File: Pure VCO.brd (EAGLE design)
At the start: 68.8 x 100 mm, 118 parts, among them IC1 TL072, IC2 TL072, IC3 TL072, IC4 TL072, IC5 TL072, IC6 TL072, IC7 TL072, IC8 LM4040A50IDBZT, T1 MMBFJ309

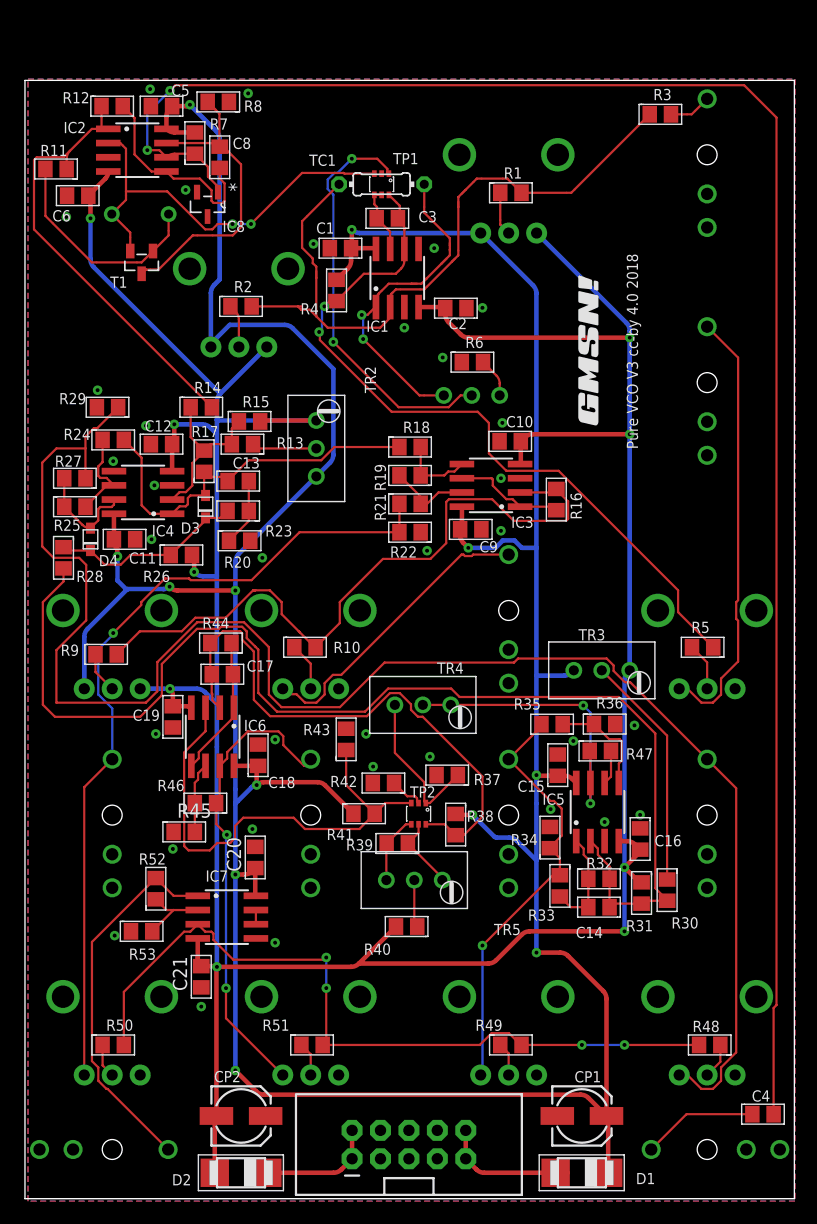
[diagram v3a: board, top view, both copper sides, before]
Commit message: VCO 3.1
VCO Updated to V3.1 14/04/21.

Mixer section changed from Average to Sum. Mix Out is now inversion of individual outs. Might be useful?
Resistor values around mixer section reduced to 10k, inline with low noise techniques.
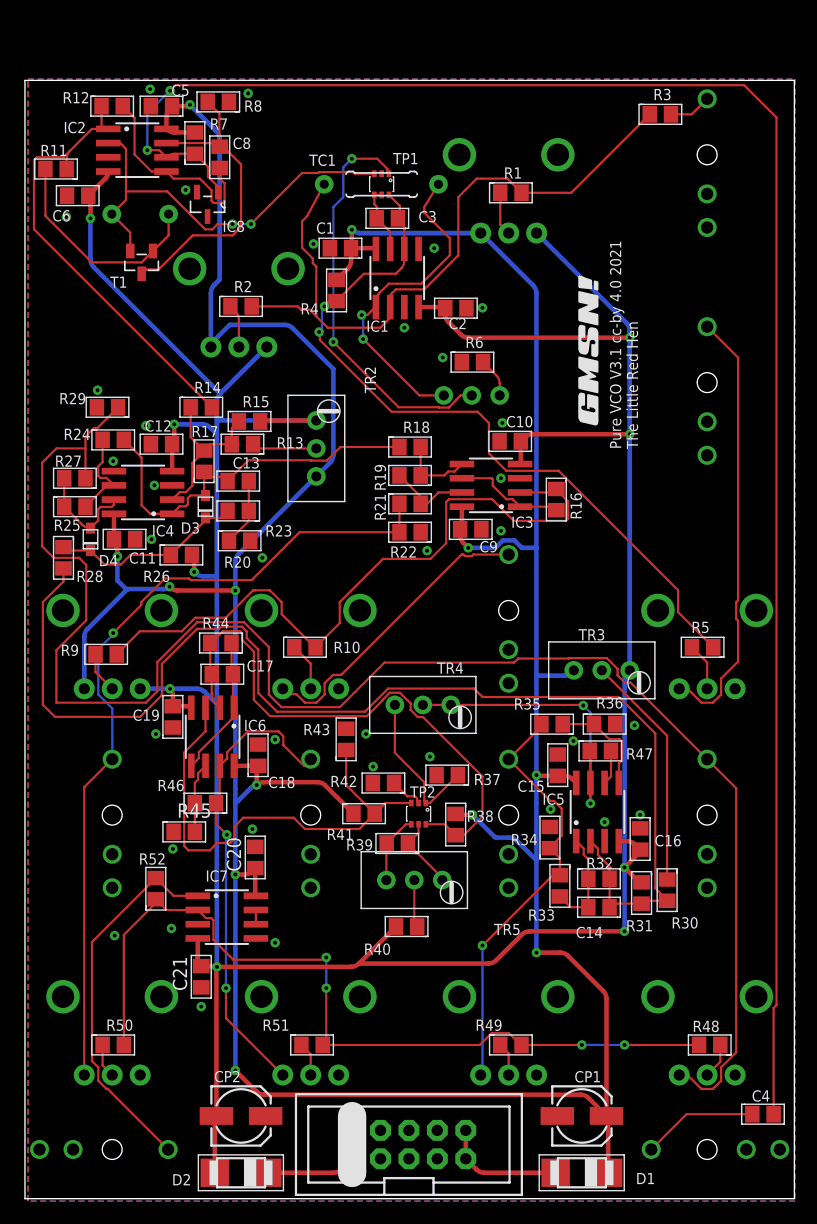
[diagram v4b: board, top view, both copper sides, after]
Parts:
- removed R53: 100k, GMSN:R0805
- COARSE: device GMSN:POTENTIOMETER_9MM -> GMSN:POT_9MM_RED_KNOB
- FINE: device GMSN:POTENTIOMETER_9MM -> GMSN:POT_9MM_RED_MXR_KNOB
- FM_LEVEL, PWM_LEVEL: device GMSN:POTENTIOMETER_9MM -> GMSN:POT_9MM_GREEN_KNOB
- PULSE_MIX, SAW_MIX, SINE_MIX, TRI_MIX: device GMSN:POTENTIOMETER_9MM -> GMSN:POT_9MM_BLUE_KNOB
- PULSE_WIDTH: device GMSN:POTENTIOMETER_9MM -> GMSN:POT_9MM_YELLOW_KNOB
- R45: value 10k -> 100k
- R46: value 19k1 -> 50k
- R47: value 1k3 -> 0R
- R48, R49, R50, R51, R52: value 100k -> 10k
- TC1: device GMSN:0204/7 -> GMSN:0207/8.5
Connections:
- removed net N$35: IC7.3, R48.2, R49.2, R50.2, R51.2
- net GND: now also IC7.3, TP1.2; no longer R53.1, TP1.B1
- net N$10: now also TP1.1; no longer TP1.B2
- net N$12: now also TP1.6; no longer TP1.C2
- net N$13: now also TP1.3; no longer TP1.C1
- net N$14: now also TP2.6; no longer TP2.C2
- net N$18: now also TP1.4, TP1.5; no longer TP1.E1, TP1.E2
- net N$48: now also R48.2, R49.2, R50.2, R51.2; no longer R53.2
- net N$76: now also TP2.1; no longer TP2.B2
- net N$77: now also TP2.5; no longer TP2.E2
- net N$78: now also TP2.4; no longer TP2.E1
- net N$80: now also TP2.2; no longer TP2.B1
- net N$82: now also TP2.3; no longer TP2.C1
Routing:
- net N$35: track 69.4 -> 0.00 mm, vias 4 -> 0
- net N$48: track 7.07 -> 75.1 mm, vias 0 -> 4
- net N$4: track 66.0 -> 62.5 mm
- net N$7: track 31.1 -> 29.7 mm
- net N$16: track 19.1 -> 18.4 mm
- net N$10: track 36.9 -> 36.4 mm
- net N$20: track 28.5 -> 28.0 mm
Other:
- board text added: "Pure VCO V3.1 cc-by 4.0 2021 The Little Red Hen"
- board text removed: "Pure VCO V3 cc-by 4.0 2018"

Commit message: Reinstall
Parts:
- removed R47: 0R, GMSN:R0805
- R7: value 87k -> 75k
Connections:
- removed net N$75: IC5.7, R47.1, TR4.1, TR4.2
- net N$19: now also IC5.7, TR4.1, TR4.2; no longer R47.2
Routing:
- net N$75: track 28.1 -> 0.00 mm, vias 2 -> 0
- net N$19: track 3.10 -> 28.8 mm, vias 0 -> 2
